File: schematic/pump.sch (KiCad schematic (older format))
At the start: 23 parts

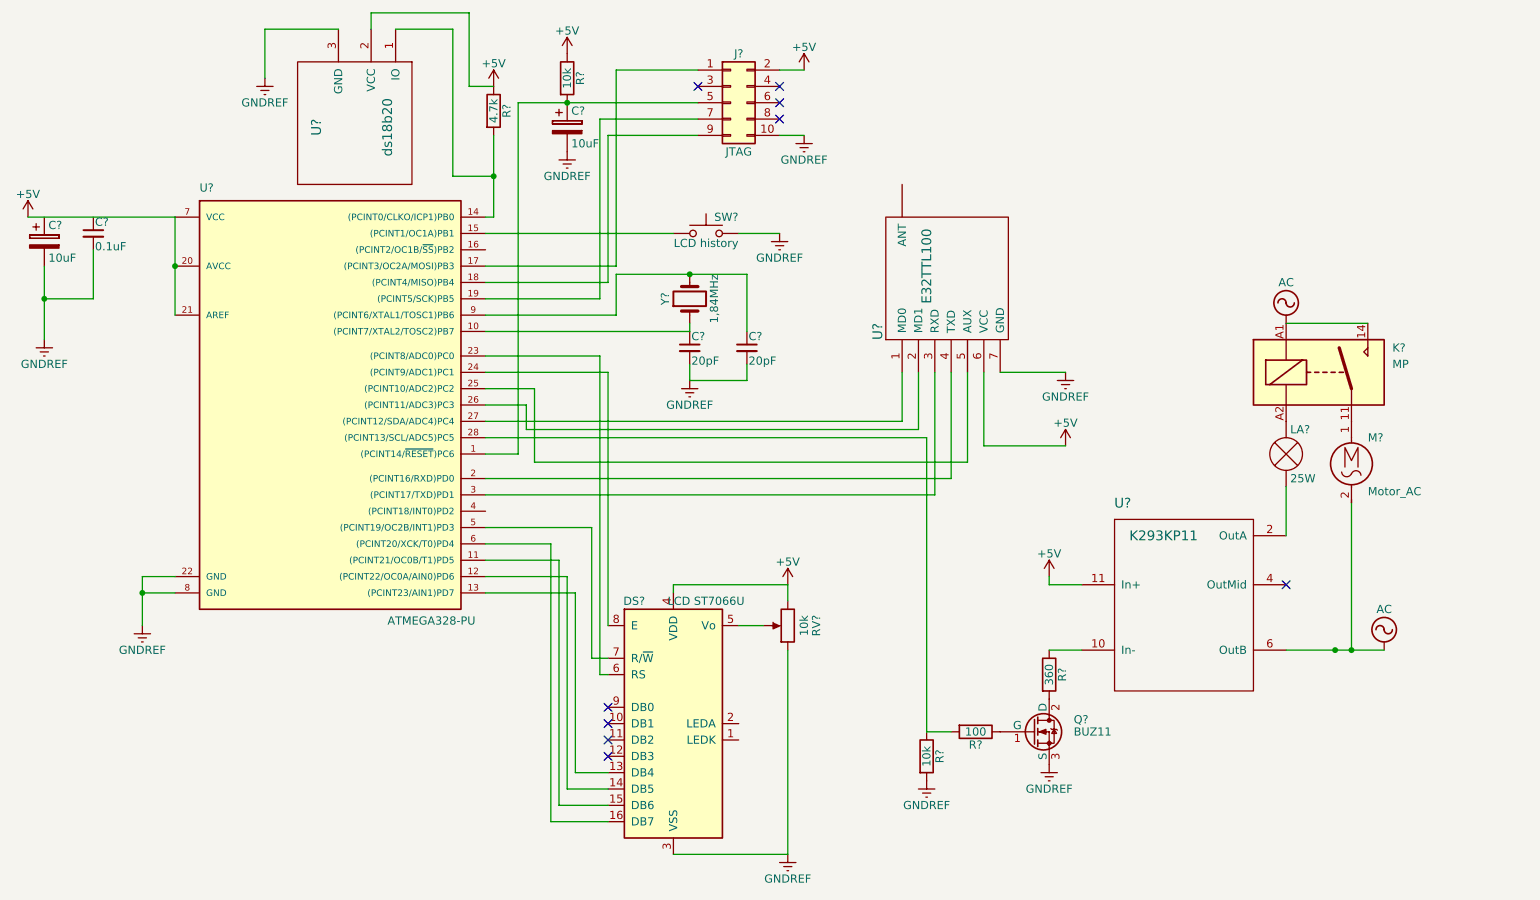
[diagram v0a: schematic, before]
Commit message: added vibrator to stop pump if MCU fails, added testplan
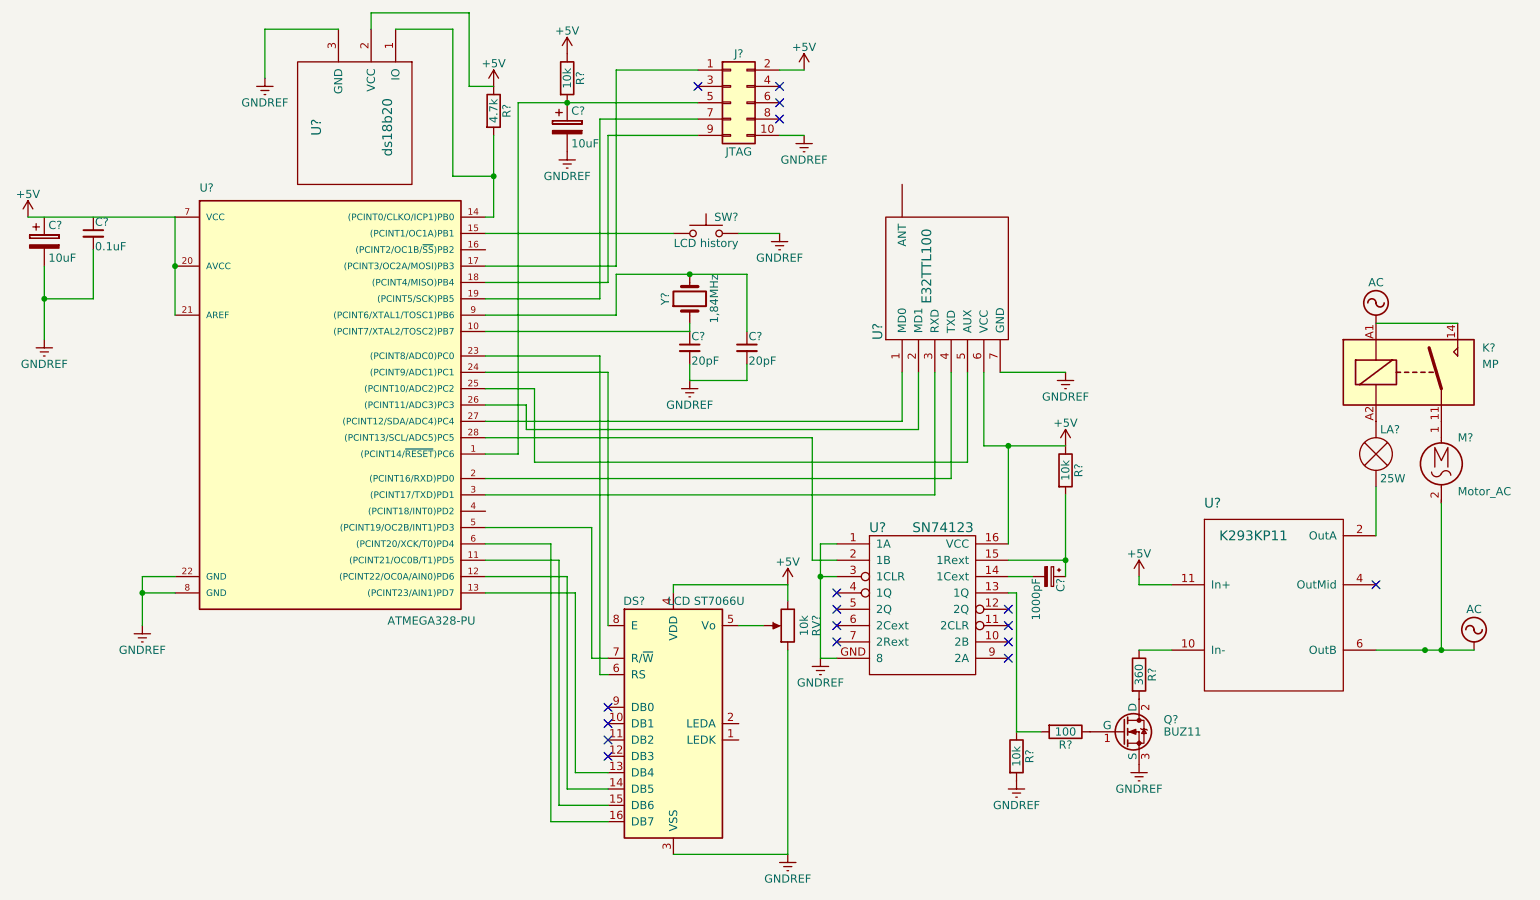
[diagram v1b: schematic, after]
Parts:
- added C?: 1000pF, symbol CP_Small
- added R?: 10k, symbol R
- added U?: SN74123, symbol SN74123
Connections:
- net +5V: now also R?.1, U?.16 (VCC)
- net GNDREF: now also U?.1 (1A), U?.3 (1CLR), U?.GND (8)
- net at R?.1, R?.2: now also U?.13 (1Q); no longer U?.28 ((PCINT13/SCL/ADC5)PC5)
- new net: U?.2 (1B), U?.28 ((PCINT13/SCL/ADC5)PC5)
- new net: C?.2, U?.14 (1Cext)
- new net: C?.1, R?.2, U?.15 (1Rext)
- no-connect marks 9 -> 17
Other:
- moved on the sheet: K?, LA?, M?, Q?, R?, U?

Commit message: Added watchdogs
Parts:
- removed C?: 1000pF, symbol CP_Small
- removed R?: 10k, symbol R
- removed U?: K293KP11, symbol K293KP11
- removed U?: SN74123, symbol SN74123
- added U?: ADM1232, symbol ADM1232
- added U?: K293KP11, symbol K293KP11
- U?: value ds18b20 -> DS18B20
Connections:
- net +5V: now also U?.11 (In+), U?.2 (TD), U?.5 (VCC)
- net AC: now also U?.6 (OutB)
- net GNDREF: now also U?.3 (Tolerance), U?.4 (GND)
- net at C?.1, J?.5 (Pin_5), R?.2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: now also U?.7 (Reset)
- net at U?.28 ((PCINT13/SCL/ADC5)PC5): now also R?.1, R?.2
- net at U?.4 ((PCINT18/INT0)PD2): now also U?.6 (Strobe)
- net at R?.1: now also U?.10 (In-)
- net at LA?.1 (-): now also U?.2 (OutA)
- no-connect marks 17 -> 11
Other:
- moved on the sheet: C?, K?, LA?, M?, Q?, R?
